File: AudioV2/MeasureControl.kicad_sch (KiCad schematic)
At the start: 101 parts, among them J1601 AUDIO, J1602 V_IN, J1603 15_V_IN, SW1601 DEST sense (3PDT 3rd pole, sa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, U1601 OPA1656, U1602 OPA1656, U1603 LT1763-3.3, U1604 MBC2596-01, U1605 TPS3307-33, U1606 LT1763-5, U1607 BP5293-50, U1608 OPA1656, U1609 XC8107AC20MR-G, U1610 MCP23017 (UI 0x22), Y1601 ASFL1-12.288MHZ-EC-T

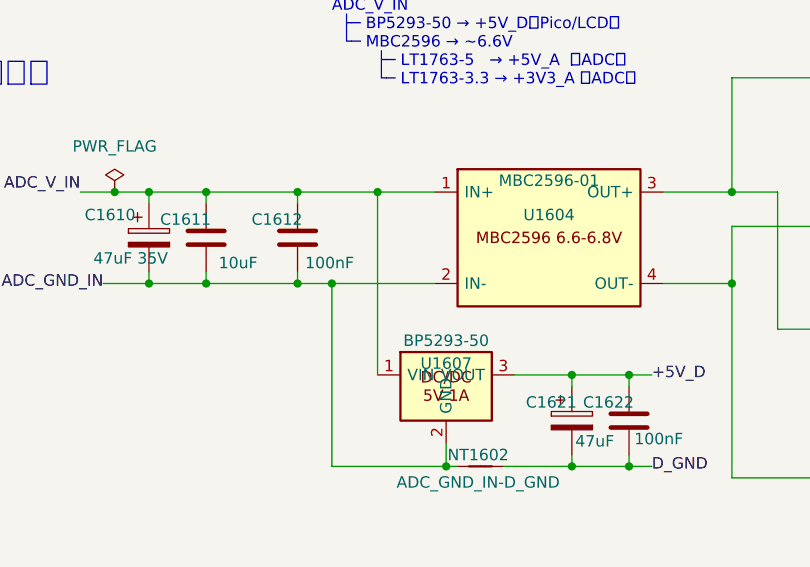
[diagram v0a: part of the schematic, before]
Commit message: AudioV2: PPTC 2個を実装（U403 / U1607 の手前）。U202 は幾何的に入らず未実装
## 実装したもの

  F202  PPTC 0.35A hold  legacy/PowerModule に置き  PD_12V_SW -> PD_12V_COIL -> U403
  F1602 PPTC 0.5A hold   MeasureControl の縦配線を分割 PD_12V_SW -> PD_12V_MEAS -> U1607

F202 は `legacy/ControlPanelAnalog` ではなく `legacy/PowerModule` に置いた。
統合後は同じシートになるのでネットは繋がるうえ、PowerModule には `Device:Fuse` が
既に埋め込まれており lib_symbols の追加が不要。電源保護が電源シートに載るのも筋が通る。
`ControlPanelAnalog` 側は `U403` の入力ラベルを `PD_12V_COIL` へ改名しただけ。

`PD_12V_COIL` / `PD_12V_MEAS` に PWR_FLAG（#FLG0202 / #FLG1602）を追加。
PPTC は受動素子なので、これが無いと KiCad が VIN を「電源が駆動していない」と判定して
ERC が 31 件に増える（実際に増えたので足した）。

## U202 前は未実装（幾何的な理由）

`+15V` の T 点 (144.78,77.47) から `U202.1` (147.32,77.47) への配線が **2.54 mm の
スタブ**で、7.62 mm の素子が入らない。T 点の上流に入れると別の枝も一緒に保護して
しまうので不可。`U202` を数 mm ずらすか引き回しを変える必要があり、それは GUI で
見ながらやる作業。30 mA の枝なので優先度は低い。DECISIONS §8 に⚠として記録した。

## ⚠ 前回の判定を訂正した（DECISIONS の記述も直した）

8c1c558 で「U403 の帰路が二次側へ戻れず通電しない」と書いたが**誤り**。
DECISIONS の A6 が結合チェーンを図示していた:

  A_GND ─NT1601─ ADC_GND ─U1604─ PD_GND ─NT1602─ MC/D_GND
                          (MBC2596 は非絶縁バック。IN- と OUT- は同一ノード)

私の解析は NetTie だけを辿って、この非絶縁バックの内部ボンドを見落としていた。
**帰路は存在した。** 問題は通電の有無ではなく経路で、リレーのパルス電流が結合
チェーン全体、つまり **ADC のアナログ星点を通って**いた。是正の価値は変わらないが、
機構の説明が間違っていたので DECISIONS の D18 実装表を訂正した。

## もう1つ見つけた（未判断）

**`U1604`（`MBC2596-01`、計測系の降圧 DC-DC）はヒューズの外。** `PD_12V_SW` に
直付けで上流は `F1601` のみ。「各コンバータの手前」を徹底するならここにも要る。
DECISIONS §8 に⚠として記録。

## 検証

- check_sexpr 13/0、sch_import --roundtrip 全6ファイル OK
- 再生成は build_daughter -> build_motherboard を2巡（CLAUDE.md の規則）
- **ERC 29 件・内訳も完全一致**（PWR_FLAG 追加前は 31 件）
- 部品 369 -> **371**（F202 / F1602。PWR_FLAG は netlist の components に出ない）
  重複 0 / 未注釈 0
- 結線を netlist で確認:
    /MotherBoard/PD_12V_COIL    = F202.2 + U403.1
    /MeasureControl/PD_12V_MEAS = F1602.2 + U1607.1
    /PD_12V_SW                  = F201.1 / F202.1 / F1602.1 + LED + SW + U1604 + caps
- gen_parts_bom --check rc=0。BOM 366 -> 368

Co-Authored-By: Claude Opus 5 <noreply@anthropic.com>
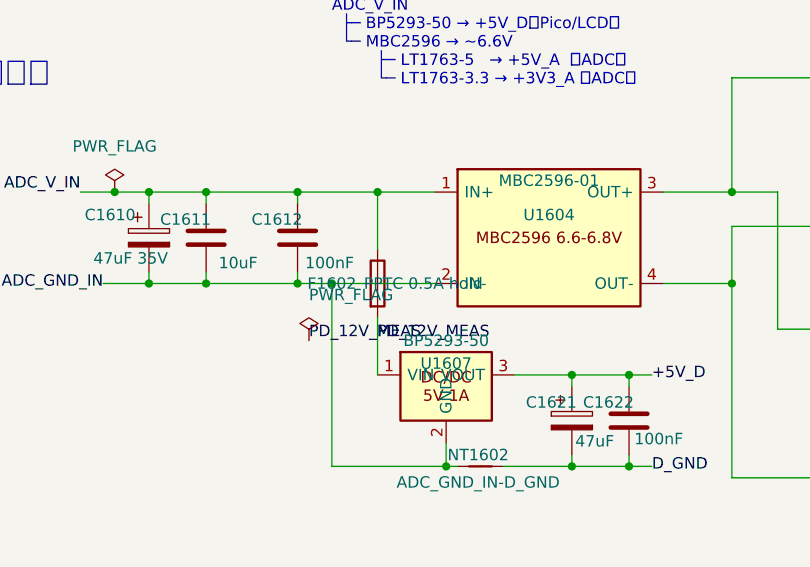
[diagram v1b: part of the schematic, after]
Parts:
- added F1602: PPTC 0.5A hold, Resistor_THT:R_Axial_DIN0411_L9.9mm_D3.6mm_P12.70mm_Horizontal, symbol Device:Fuse
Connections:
- net ADC_V_IN: now also F1602.1; no longer U1607.1 (VIN)
- new net PD_12V_MEAS: F1602.2, U1607.1 (VIN)
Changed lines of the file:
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@@
 	(wire
 		(pts
-			(xy 262.89 44.45) (xy 262.89 64.77)
-		)
-		(stroke
-			(width 0)
-			(type default)
-		)
-	)
-	(wire
-		(pts
 			(xy 193.04 73.66) (xy 193.04 78.74)
 		)
@@
 		)
 	)
+	(symbol
+		(lib_id "Device:Fuse")
+		(at 262.89 54.61 0)
+		(unit 1)
+		(body_style 1)
+		(exclude_from_sim no)
+		(in_bom yes)
+		(on_board yes)
+		(in_pos_files yes)
+		(dnp no)
+		(property "Reference" "F1602"
+			(at 257.81 54.61 0)
+			(show_name no)
+			(do_not_autoplace no)
+			(effects
+				(font
+					(size 1.27 1.27)
+				)
+			)
+		)
+		(property "Value" "PPTC 0.5A hold"
+			(at 267.97 54.61 0)
+			(show_name no)
+			(do_not_autoplace no)
+			(effects
+				(font
+					(size 1.27 1.27)
+				)
+			)
+		)
+		(property "Footprint" "Resistor_THT:R_Axial_DIN0411_L9.9mm_D3.6mm_P12.70mm_Horizontal"
+			(at 67.818 223.52 90)
+			(hide yes)
+			(show_name no)
+			(do_not_autoplace no)
+			(effects
+				(font
+					(size 1.27 1.27)
+				)
+			)
+		)
+		(property "Datasheet" ""
+			(at 66.04 223.52 0)
+			(hide yes)
+			(show_name no)
+			(do_not_autoplace no)
+			(effects
+				(font
+					(size 1.27 1.27)
+				)
+			)
+		)
+		(property "Description" "Fuse"
+			(at 66.04 223.52 0)
+			(hide yes)
+			(show_name no)
+			(do_not_autoplace no)
+			(effects
+				(font
+					(size 1.27 1.27)
+				)
+			)
+		)
+		(pin "2"
+		)
+		(pin "1"
+		)
+		(instances
+			(project "AudioV2Case"
+				(path "/a1000001-0001-4001-8001-000000000001/43e41fda-fe26-43e3-950a-c017f3070bbf"
+					(reference "F1602")
+					(unit 1)
+				)
+			)
+		)
+	)
+	(wire
+		(pts
+			(xy 262.89 44.45) (xy 262.89 50.8)
+		)
+		(stroke
+			(width 0)
+			(type default)
+		)
+	)
+	(wire
+		(pts
+			(xy 262.89 58.42) (xy 262.89 64.77)
+		)
+		(stroke
+			(width 0)
+			(type default)
+		)
+	)
+	(label "PD_12V_MEAS"
+		(at 262.89 60.96 0)
+		(effects
+			(font
+				(size 1.27 1.27)
+			)
+			(justify left bottom)
+		)
+	)
+	(symbol
+		(lib_id "power:PWR_FLAG")
+		(at 255.27 60.96 0)
+		(unit 1)
+		(body_style 1)
+		(exclude_from_sim no)
+		(in_bom yes)
+		(on_board yes)
+		(in_pos_files yes)
+		(dnp no)
+		(fields_autoplaced yes)
+		(property "Reference" "#FLG1602"
+			(at 255.27 58.42 0)
+			(hide yes)
+			(show_name no)
+			(do_not_autoplace no)
+			(effects
+				(font
+					(size 1.27 1.27)
+				)
+			)
+		)
+		(property "Value" "PWR_FLAG"
+			(at 255.27 55.88 0)
+			(show_name no)
+			(do_not_autoplace no)
+			(effects
+				(font
+					(size 1.27 1.27)
+				)
+				(justify left)
+			)
+		)
+		(property "Footprint" ""
+			(at 266.7 125.73 0)
+			(hide yes)
+			(show_name no)
+			(do_not_autoplace no)
+			(effects
+				(font
+					(size 1.27 1.27)
+				)
+			)
+		)
+		(property "Datasheet" ""
+			(at 266.7 125.73 0)
+			(hide yes)
+			(show_name no)
+			(do_not_autoplace no)
+			(effects
+				(font
+					(size 1.27 1.27)
+				)
+			)
+		)
+		(property "Description" "Special symbol for telling ERC where power comes from"
+			(at 266.7 125.73 0)
+			(hide yes)
+			(show_name no)
+			(do_not_autoplace no)
+			(effects
+				(font
+					(size 1.27 1.27)
+				)
+			)
+		)
+		(pin "1"
+		)
+		(instances
+			(project "AudioV2Case"
+				(path "/a1000001-0001-4001-8001-000000000001/43e41fda-fe26-43e3-950a-c017f3070bbf"
+					(reference "#FLG1602")
+					(unit 1)
+				)
+			)
+		)
+	)
+	(label "PD_12V_MEAS"
+		(at 255.27 60.96 0)
+		(effects
+			(font
+				(size 1.27 1.27)
+			)
+			(justify left bottom)
+		)
+	)

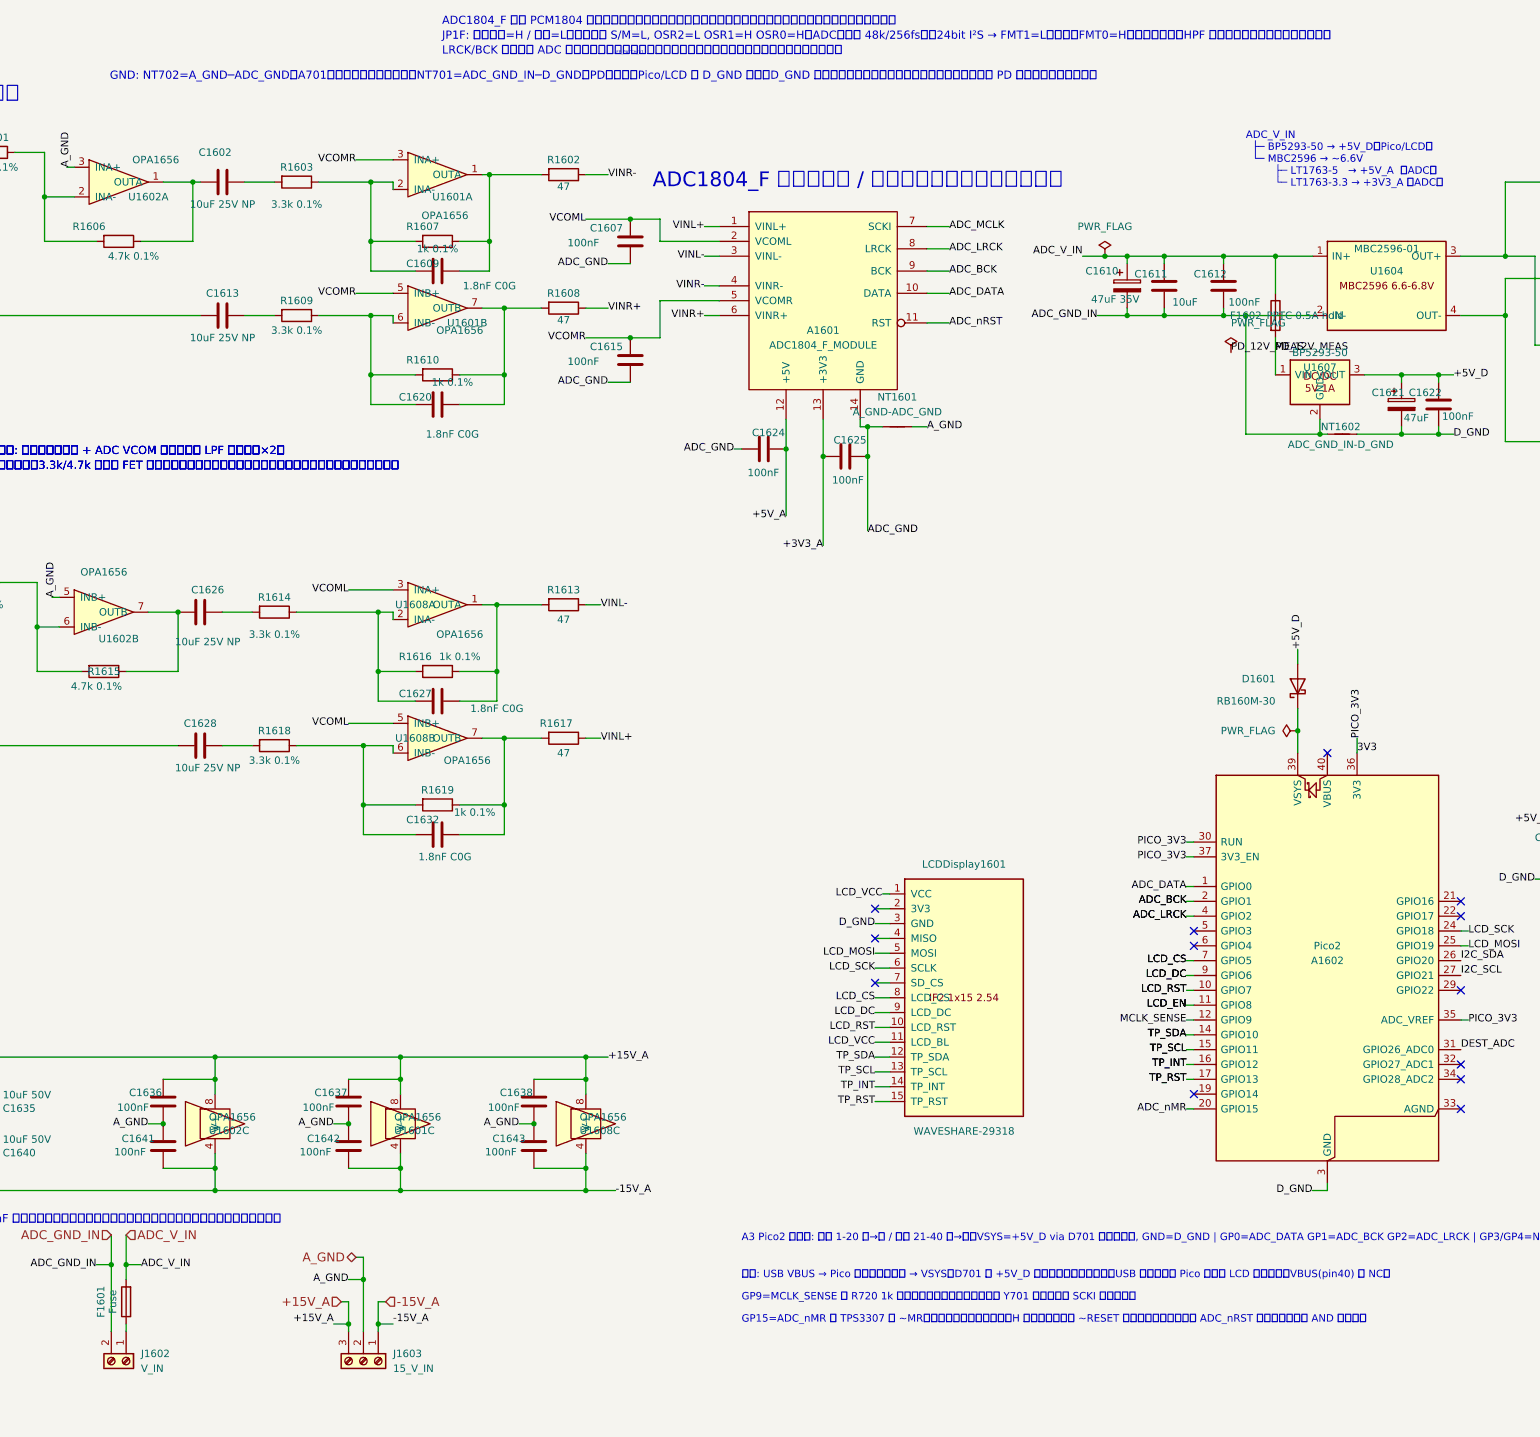
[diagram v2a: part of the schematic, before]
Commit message: AudioV2: D-g を実装した。U1604 の手前に PPTC 0.15A とローカルバルク
`MeasureControl` に追加:

| | |
|---|---|
| `F1603` | PPTC 0.15A hold を `(265.43, 34.29)` r90 |
| `C1644` | ローカルバルク 47µF 35V。**ヒューズの下流** |
| `#FLG1603` | PWR_FLAG |
| `PD_12V_ADC` | ヒューズ下流の新ネット |
| `F1601` の Value | `"Fuse"` → **`T1A slow`**（定格が入っていなかった） |

**走行線の上へ迂回した。** `ADC_V_IN` から `U1604` の IN+ までは直線で 6.35mm しか無く、
7.62mm のヒューズが入らない（**D-f が止まっているのと同じ理由**）。上を回して解決したので、
D-f にも同じ手が使えるかもしれない旨を書き添えた。

**バルクはヒューズの下流に置いた。** PPTC は 2〜5Ω あるので、コンバータの入力パルスを
共通バルクからヒューズ越しに引くと意味が薄れる。手前で供給する。

検証:
- **ネットリストの分割の差分は狙った1点だけ** —— `U1604.1` が `PD_12V_SW` から
  `PD_12V_ADC` へ移った。それ以外は完全一致
- ERC 29件で実装前と同一。部品 371→**373**・重複0・注釈警告なし
- check_sexpr 問題0、roundtrip OK

途中で2回踏んだので記録した:

1. **参照番号を「最大値＋1」で採って既存と衝突した。** `C16xx` は C1601-C1643 と
   C1650 が使用中で**ギャップがある**。`C1613` は既に居た。空き番号は列挙して確かめる
2. **PPTC を直列に入れると `power_pin_not_driven` が出る。** 受動素子なので切れた下流に
   駆動源が居なくなる。`PWR_FLAG` が要る（`F1602` の `#FLG1602` と同じ）。ERC 30→29 に戻った

なお重複判定は「同じ参照が複数ある」では出せない —— マルチユニット部品
（U1601/U1602/U1608）は同じ参照で複数ブロックを持つのが正しい。`(unit N)` で見る。

📌 フットプリントは `F1602` に合わせて軸型 12.70mm ピッチにしてある。**PPTC の実物は
普通ラジアルのディスク**なので、部品選定時に見直すこと（`F1602` も同じ）。

Co-Authored-By: Claude Opus 5 <noreply@anthropic.com>
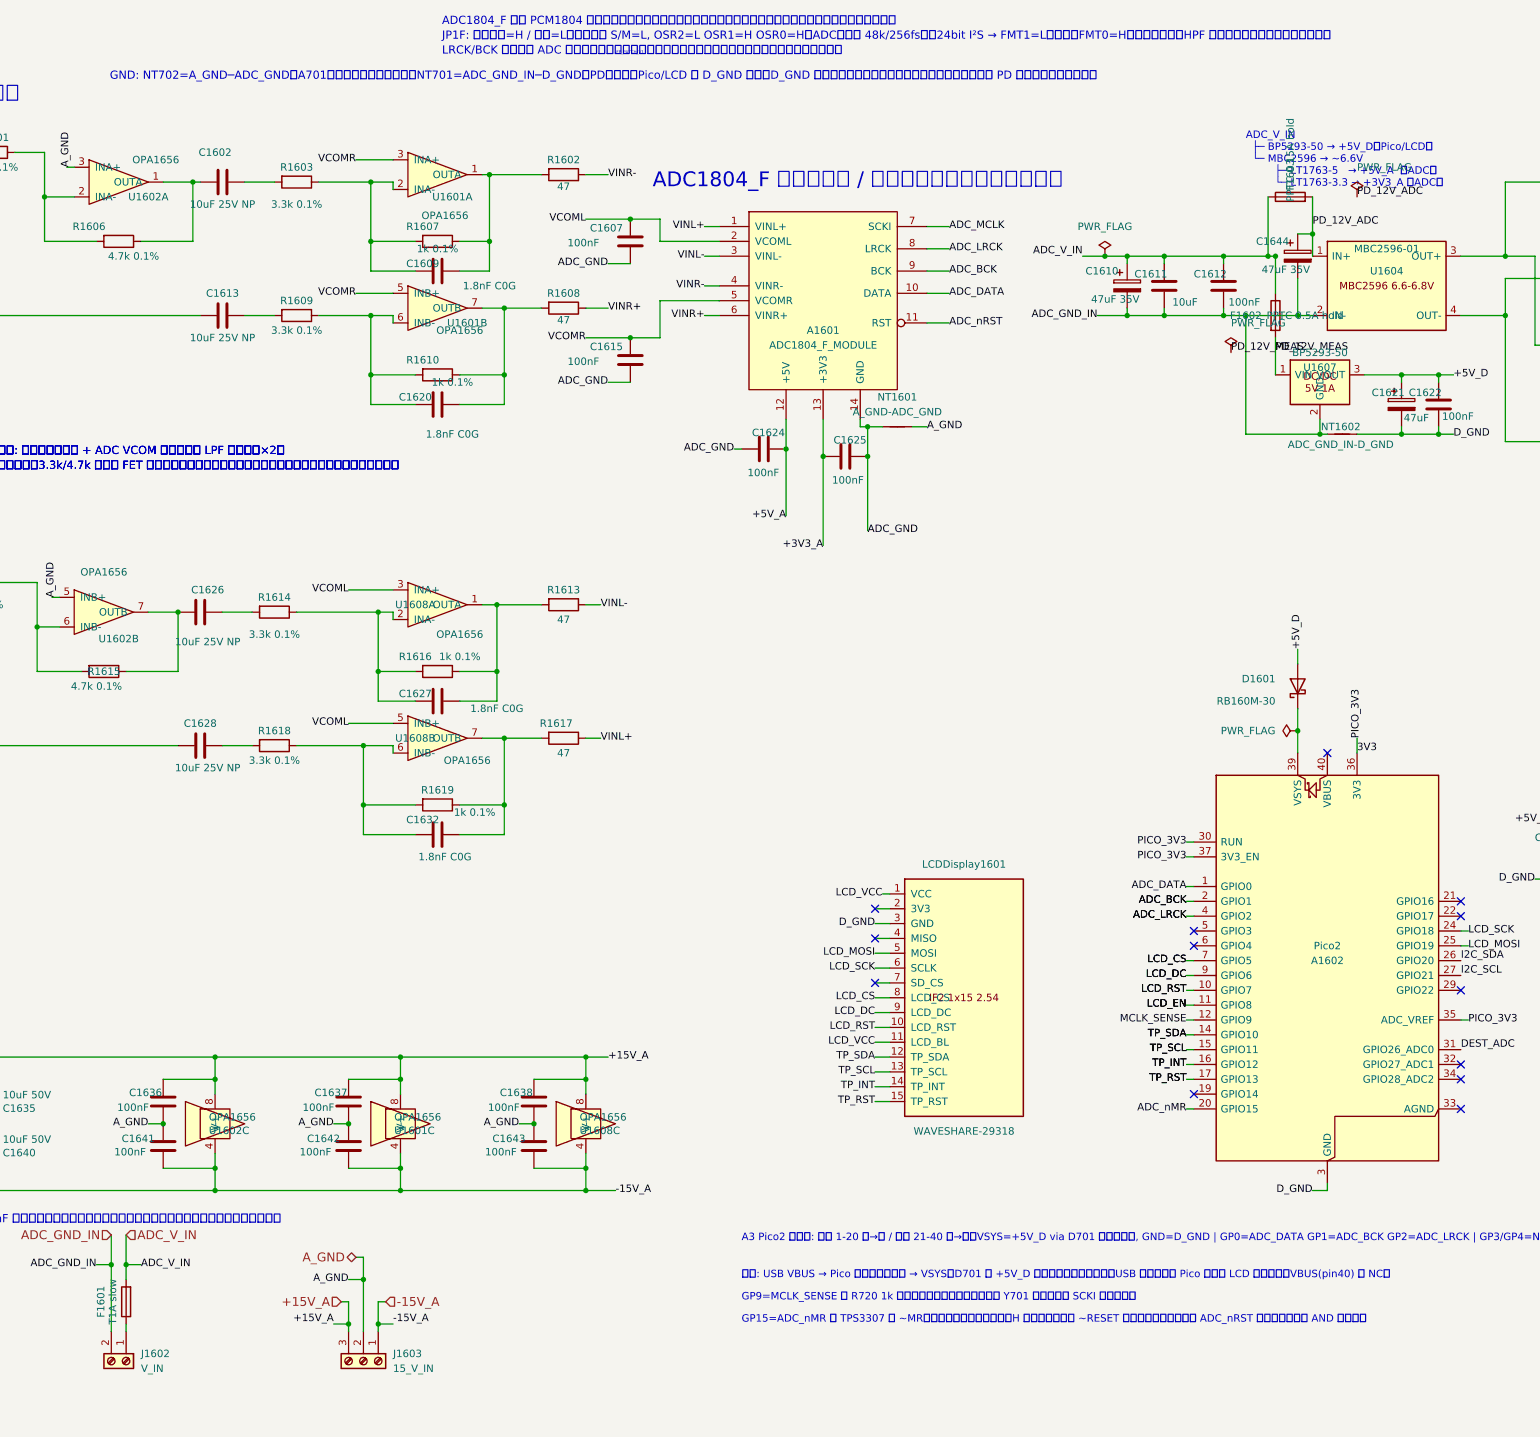
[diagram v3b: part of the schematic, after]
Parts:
- added C1644: 47uF 35V, Capacitor_THT:CP_Radial_D8.0mm_P3.50mm, symbol Device:C_Polarized
- added F1603: PPTC 0.15A hold, Resistor_THT:R_Axial_DIN0411_L9.9mm_D3.6mm_P12.70mm_Horizontal, symbol Device:Fuse
- F1601: value Fuse -> T1A slow
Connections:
- net ADC_GND_IN: now also C1644.2
- net ADC_V_IN: now also F1603.1; no longer U1604.1 (IN+)
- new net PD_12V_ADC: C1644.1, F1603.2, U1604.1 (IN+)

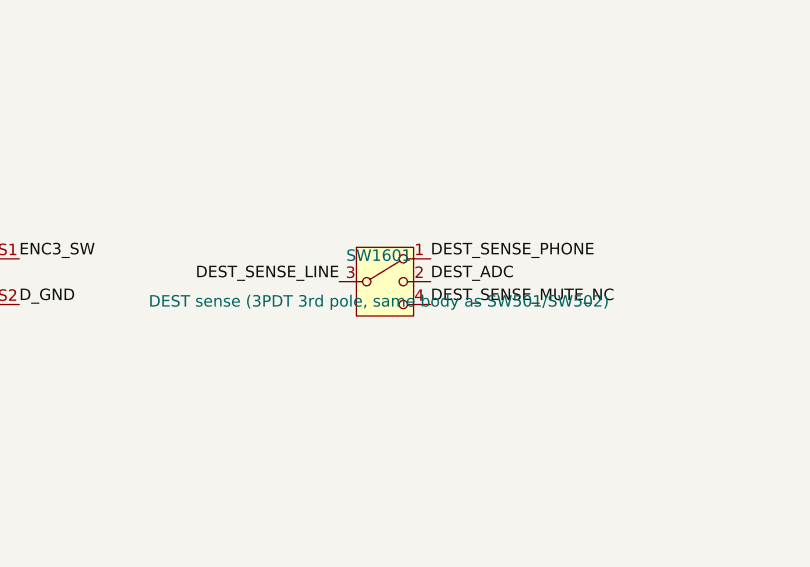
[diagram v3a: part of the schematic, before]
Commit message: AudioV2: SW1601 のコモン端子を直した（PHONE が検出できなかった）
Switch:SW_SP3T のコモンは pin 3（シンボル本体で x=-5.08 に1本だけ、
他3本は +5.08 の投げ先）。音声側の SW501/SW502 は pin 3 に AMP_SEL_L/R
を置いていたが、同じスイッチ体の3極目 SW1601 だけ pin 3 に
DEST_SENSE_LINE、pin 2 に DEST_ADC を置いていた。

ADC ノードが投げ先側にあると、3ポジションのうち1つでしか ADC に触らない。
残り2つは 10k/10k の中点のままで、3ポジションが2値にしか化けない。

  旧  pin1 PHONE -> 1.650V (MUTE と同値)
      pin2 ADC   -> 3.025V
      pin4 開放  -> 1.650V
  → PHONE が絶対に検出できない

DEST_SENSE_LADDER.md が「ADC はコモン」「LINE 3.025 / MUTE 1.650 /
PHONE 0.275 V」と明記しており、設計意図からの逸脱で確定。

SW501/SW502 と同じ並びに揃えた:
  pin1 DEST_SENSE_PHONE（変更なし）
  pin2 DEST_SENSE_MUTE_NC（中央=MUTE）
  pin3 DEST_ADC（コモン）
  pin4 DEST_SENSE_LINE

MeasureControl は手編集所有。SW1601 のピン先はラベル直置きで、ワイヤは
1本も触れていないことを座標で確認してからラベルだけ張り替えた。
シートピンは増減していないので build_motherboard.py の CHILD_SHEETS は
そのまま。

検証:
  ラダー電圧  LINE 3.025 / MUTE 1.650 / PHONE 0.275 V（仕様と一致）
  DEST_ADC    A1602.31 / R1656.2 / R1657.1 / SW1601.3
  erc         17 件（変化なし）
  netlist     部品 369 / 重複 0（変化なし）
  check_sexpr 13 ファイル / 問題 0
  roundtrip   OK

指摘は sch-review エージェント。回路図まで降ろして裏を取ってから適用した。

Co-Authored-By: Claude Opus 5 <noreply@anthropic.com>
Claude-Session: https://claude.ai/code/session_01VCArLcCGbMGgxvWJ5HFJiY
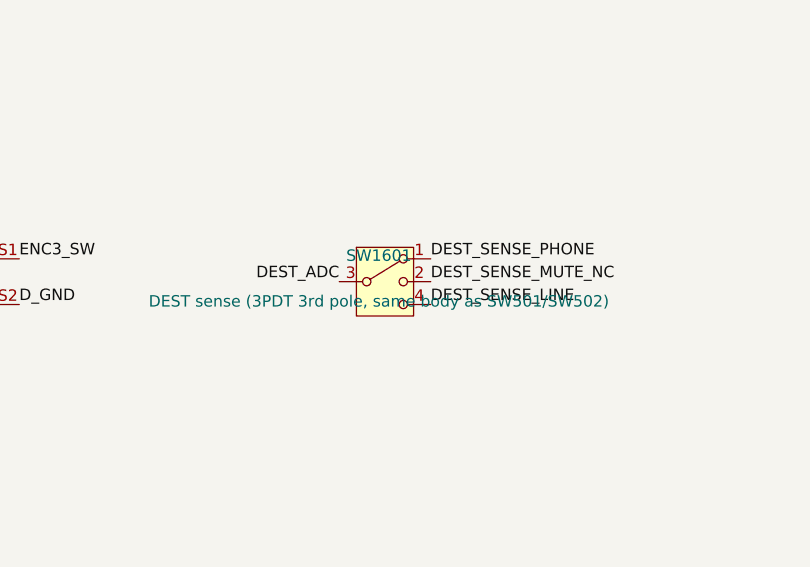
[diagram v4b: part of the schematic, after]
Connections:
- net DEST_ADC: now also SW1601.3; no longer SW1601.2
- net DEST_SENSE_LINE: now also SW1601.4; no longer SW1601.3
- net DEST_SENSE_MUTE_NC: now also SW1601.2; no longer SW1601.4
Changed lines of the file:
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@@
 		)
 	)
-	(label "DEST_SENSE_MUTE_NC"
+	(label "DEST_SENSE_LINE"
 		(at 365.76 342.9 0)
 		(effects
@@
 		)
 	)
-	(label "DEST_ADC"
+	(label "DEST_SENSE_MUTE_NC"
 		(at 365.76 340.36 0)
 		(effects
@@
 		)
 	)
-	(label "DEST_SENSE_LINE"
+	(label "DEST_ADC"
 		(at 355.6 340.36 180)
 		(effects
